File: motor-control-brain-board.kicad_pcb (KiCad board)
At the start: 4 copper layers, 60 x 50 mm, 110 parts, among them J1 GPIO, J10 PWM, J11 PWR, J12 POWER_SENSE, J13 MISC_SENSE, J2 I2C, J3 SERIAL_1, J4 SERIAL_2, J5 CAN, J6 SPI, J7 USB_C_Receptacle_USB2.0_16P, J8 SWD, J9 POS_SENSE, SW1 RST, U1 TLV76750QWDRBxQ1, U10 TLV9061xDCK, U11 TLV9061xDCK, U13 TLV9061xDCK, U2 TLV76733QWDRBxQ1, U3 M95256-RDW6TP, U4 STM32G474RETx, U5 TCAN1044V-Q1, U6 TLV9061xDCK, U7 TLV9061xDCK, U8 TLV9061xDCK, U9 TLV9061xDCK, Y1 ECS-160-20-33-DU-TR

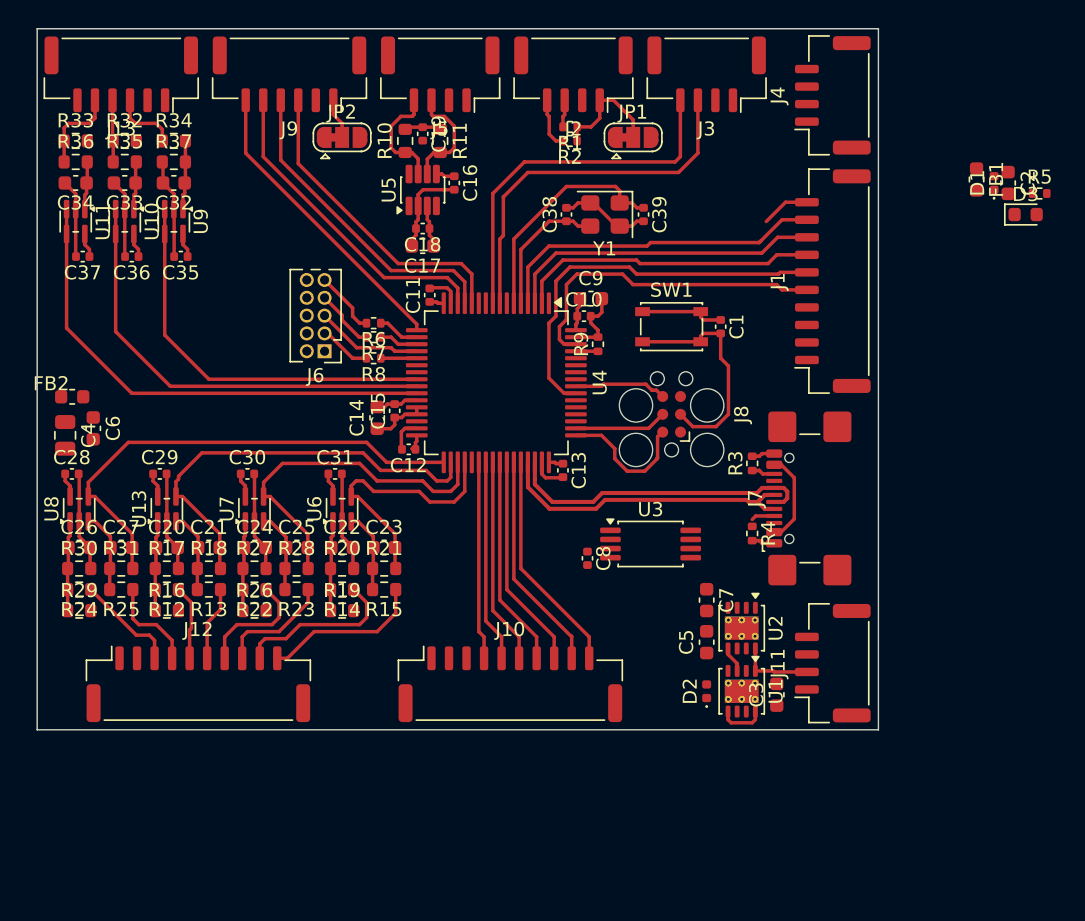
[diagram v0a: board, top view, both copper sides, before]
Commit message: Updating all decoupling to 1u
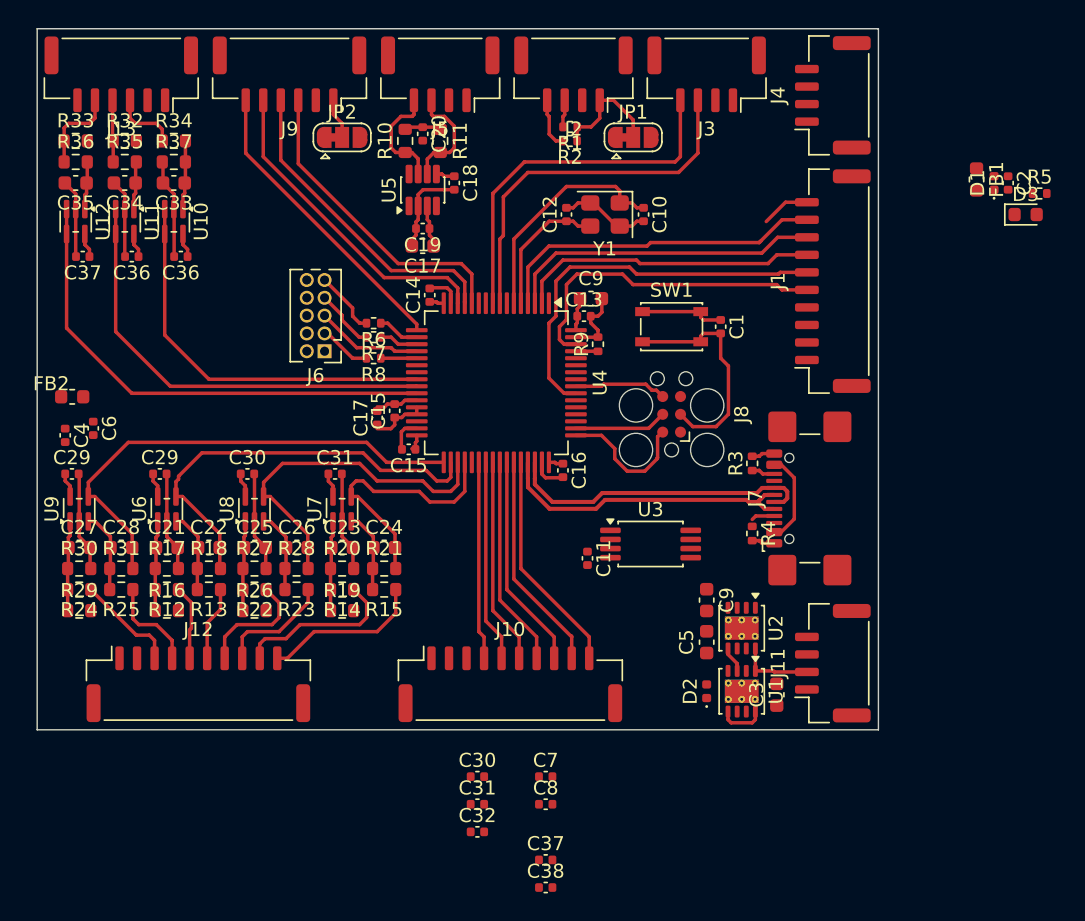
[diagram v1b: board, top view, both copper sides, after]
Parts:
- added C30: 1u, Capacitor_SMD:C_0402_1005Metric, F.Cu at (151.4, 123.3)
- added C31: 1u, Capacitor_SMD:C_0402_1005Metric, F.Cu at (151.4, 125.3)
- added C32: 1u, Capacitor_SMD:C_0402_1005Metric, F.Cu at (151.4, 127.3)
- added C37: 1u, Capacitor_SMD:C_0402_1005Metric, F.Cu at (156.3, 129.3)
- added C38: 1u, Capacitor_SMD:C_0402_1005Metric, F.Cu at (156.3, 131.2)
- added C7: 1u, Capacitor_SMD:C_0402_1005Metric, F.Cu at (156.3, 123.3)
- added C8: 1u, Capacitor_SMD:C_0402_1005Metric, F.Cu at (156.3, 125.3)
- C1: value 100n -> 1u
- C11: renamed from C8; value 100n -> 1u
- C13: renamed from C10; value 100n -> 1u
- C14: renamed from C11; value 100n -> 1u
- C15: renamed from C12; value 100n -> 1u
- C16: renamed from C13; value 100n -> 1u
- C17: renamed from C14; footprint Capacitor_SMD:C_0603_1608Metric -> Capacitor_SMD:C_0402_1005Metric
- C18: renamed from C16; value 100n -> 1u
- C19: renamed from C18; value 100n -> 1u
- C2, C6: footprint Capacitor_SMD:C_0603_1608Metric -> Capacitor_SMD:C_0402_1005Metric
- C29: renamed from C28; value 100n -> 1u
- C3, C5: value 1u -> 2u2
- C36: renamed from C35; value 100n -> 1u
- C4: value 22u -> 1u; footprint Capacitor_SMD:C_0805_2012Metric -> Capacitor_SMD:C_0402_1005Metric
- C9: renamed from C7; value 1u -> 2u2
- renumbered C39 to C10, C38 to C12, C19 to C20, C20 to C21, C21 to C22, C22 to C23, C23 to C24, C24 to C25, C25 to C26, C26 to C27, C27 to C28, C32 to C33, C33 to C34, C34 to C35, U9 to U10, U10 to U11, U11 to U12, U13 to U6, U6 to U7, U7 to U8, U8 to U9

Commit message: did stuff
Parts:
- removed the C15 at (145.5, 97.2)
- removed the C17 at (147.5, 85.5)
- removed the C29 at (128.8, 101.8)
- removed the C30 at (135.0, 101.8)
- removed the C31 at (141.2, 101.8)
- removed the C36 at (126.8, 86.2)
- removed the C37 at (123.2, 86.2)
- removed the C9 at (159.5, 89.2)
- moved C38 55.8 mm to (123.2, 86.2), turned to 180 degrees
- moved C37 52.2 mm to (126.8, 86.2), turned to 180 degrees
- moved C7 40.7 mm to (125.7, 96.5)
- moved C8 40.7 mm to (125.7, 98.5)
- moved FB1 32.5 mm to (170.5, 108.8), turned to 90 degrees
- moved C30 31.3 mm to (128.7, 101.8)
- moved C31 28.7 mm to (135.0, 101.8)
- moved C32 27.5 mm to (141.2, 101.8)
- moved C11 6.82 mm to (158.2, 101.0)
- moved U3 6.82 mm to (162.8, 100.0)
- moved J8 5.48 mm to (163.0, 92.5)
- moved C13 4.83 mm to (154.5, 88.8)
- moved C14 4.83 mm to (143.5, 87.2)
- moved C15 4.83 mm to (142.0, 98.2)
- moved C16 4.83 mm to (153.0, 99.8)
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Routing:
- net /USB_D+: track 22.1 -> 27.9 mm
- net /USB_D-: track 22.1 -> 27.9 mm
- net /POS_A: track 22.2 -> 16.7 mm
- net /POS_B: track 22.6 -> 17.3 mm
- net /CURR_B: track 24.8 -> 19.5 mm
- net /POS_C/RES_OUT: track 22.9 -> 17.7 mm
- net /CURR_A: track 30.4 -> 25.2 mm
- net /ACC: track 28.3 -> 23.2 mm
- net /CURR_C: track 18.7 -> 13.7 mm
- net /THM_1: track 31.9 -> 27.1 mm
- net GND: track 84.6 -> 80.1 mm
- net /NRST: track 16.2 -> 11.7 mm
- net /THM_2: track 35.4 -> 31.0 mm
- net /VOLT_DC: track 34.9 -> 30.5 mm
- net /UART2_TX: track 6.62 -> 10.5 mm
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
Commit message: did stuff
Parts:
- moved R12 1.50 mm to (129.2, 111.5)
- moved R14 1.50 mm to (141.8, 111.5)
- moved R16 1.50 mm to (129.2, 110.0)
- moved R19 1.50 mm to (141.8, 110.0)
- moved R22 1.50 mm to (135.5, 111.5)
- moved R24 1.50 mm to (123.0, 111.5)
- moved R26 1.50 mm to (135.5, 110.0)
- moved R29 1.50 mm to (123.0, 110.0)
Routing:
- net GND: track 80.1 -> 88.8 mm
- net +12V: track 3.29 -> 10.5 mm
- net +3V3: track 5.50 -> 11.7 mm
- net +5V: track 8.85 -> 12.8 mm
- net /CURR_C+: track 11.8 -> 8.71 mm
- net /CURR_B+: track 8.35 -> 5.25 mm
- net /CURR_A+: track 5.33 -> 3.73 mm
- net /VOLT_DC+: track 7.33 -> 6.71 mm
